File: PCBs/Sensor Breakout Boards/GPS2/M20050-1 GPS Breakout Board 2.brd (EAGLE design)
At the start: 26.7 x 35.6 mm, 8 parts, among them J1 2X6 FEMALE

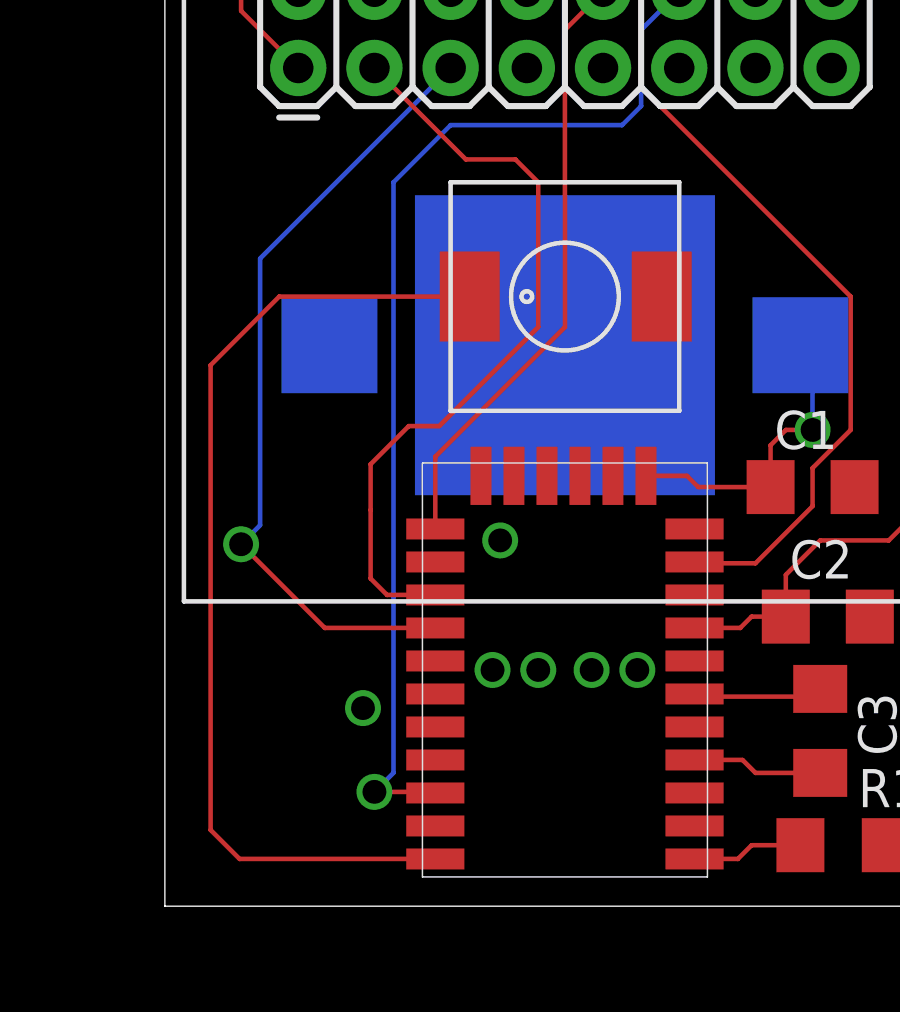
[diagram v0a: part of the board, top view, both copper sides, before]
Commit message: update gps to work with smaller inductor
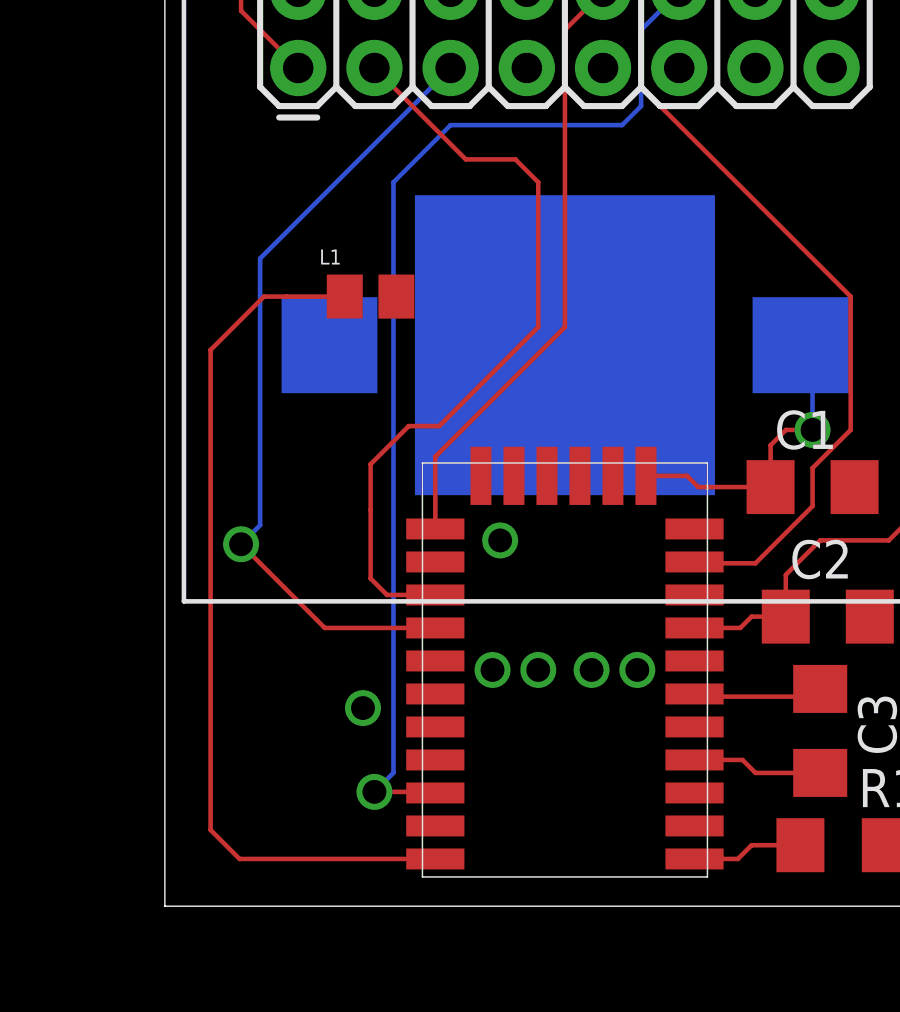
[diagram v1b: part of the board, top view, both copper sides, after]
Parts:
- L1: device RTR Main Library:L-DS75LC -> AIMC-0805-1N8S-T:INDC2012X105N
- moved L1 6.48 mm to (6.86, 20.3)
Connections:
- net GND: now also L1.2; no longer L1.P$2
- net N$4: now also L1.1; no longer L1.P$1
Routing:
- net N$4: track 33.0 -> 29.1 mm
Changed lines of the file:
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@@
 <attribute name="VALUE" x="21.336" y="-0.508" size="1.27" layer="27"/>
 </element>
-<element name="L1" library="RTR Main Library" package="L-DS75LC" value="1.8n" x="13.335" y="20.32" smashed="yes"/>
+<element name="L1" library="AIMC-0805-1N8S-T" package="INDC2012X105N" value="1.8n" x="6.858" y="20.32" smashed="yes">
+<attribute name="DESCRIPTION" value=" IND 1.8nH 0.3A 100mΩ " x="6.858" y="20.32" size="1.778" layer="27" display="off"/>
+<attribute name="DIGI-KEY_PART_NUMBER" value="535-11559-1-ND" x="6.858" y="20.32" size="1.778" layer="27" display="off"/>
+<attribute name="MF" value="Abracon" x="6.858" y="20.32" size="1.778" layer="27" display="off"/>
+<attribute name="MP" value="AIMC-0805-1N8S-T" x="6.858" y="20.32" size="1.778" layer="27" display="off"/>
+<attribute name="NAME" x="5.148" y="21.39" size="0.5" layer="25"/>
+<attribute name="PACKAGE" value="2012 Bourns" x="6.858" y="20.32" size="1.778" layer="27" display="off"/>
+<attribute name="PURCHASE-URL" value="https://pricing.snapeda.com/search/part/AIMC-0805-1N8S-T/?ref=eda" x="6.858" y="20.32" size="1.778" layer="27" display="off"/>
+<attribute name="VALUE" x="5.148" y="19.25" size="0.5" layer="27" align="top-left"/>
+</element>
 </elements>
 <signals>
@@
 <contactref element="C2" pad="2"/>
 <contactref element="R1" pad="2"/>
-<contactref element="L1" pad="P$2"/>
 <polygon width="0.1524" layer="1">
 <vertex x="-6.35" y="39.37"/>
@@
 <via x="11.176" y="12.192" extent="1-16" drill="0.79375"/>
 <via x="6.604" y="6.604" extent="1-16" drill="0.79375"/>
+<contactref element="L1" pad="2"/>
 </signal>
 <signal name="N$1">
@@
 <signal name="N$4">
 <contactref element="A1" pad="P28"/>
-<contactref element="L1" pad="P$1"/>
 <wire x1="9.015" y1="1.574" x2="2.49" y2="1.574" width="0.1524" layer="1"/>
 <wire x1="2.49" y1="1.574" x2="1.524" y2="2.54" width="0.1524" layer="1"/>
-<wire x1="1.524" y1="2.54" x2="1.524" y2="18.034" width="0.1524" layer="1"/>
-<wire x1="1.524" y1="18.034" x2="3.81" y2="20.32" width="0.1524" layer="1"/>
-<wire x1="3.81" y1="20.32" x2="10.16" y2="20.32" width="0.1524" layer="1"/>
+<wire x1="1.524" y1="2.54" x2="1.524" y2="18.542" width="0.1524" layer="1"/>
+<wire x1="1.524" y1="18.542" x2="3.302" y2="20.32" width="0.1524" layer="1"/>
+<contactref element="L1" pad="1"/>
+<wire x1="3.302" y1="20.32" x2="4.064" y2="20.32" width="0.1524" layer="1"/>
+<wire x1="4.064" y1="20.32" x2="5.998" y2="20.32" width="0.1524" layer="1"/>
+<wire x1="4.064" y1="20.32" x2="4.064" y2="20.32" width="0.1524" layer="1"/>
 </signal>
 <signal name="TX">
